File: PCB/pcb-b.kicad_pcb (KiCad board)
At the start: 2 copper layers, 109.8 x 43.6 mm, 93 parts, among them J1 IXTP3N50D2, Q1 BC817, Q10 BC817, Q11 TPCA8120,L1Q, Q12 BC817, Q13 TPCA8120,L1Q, Q14 BC817, Q15 BC817, Q16 BC817, Q17 BC327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

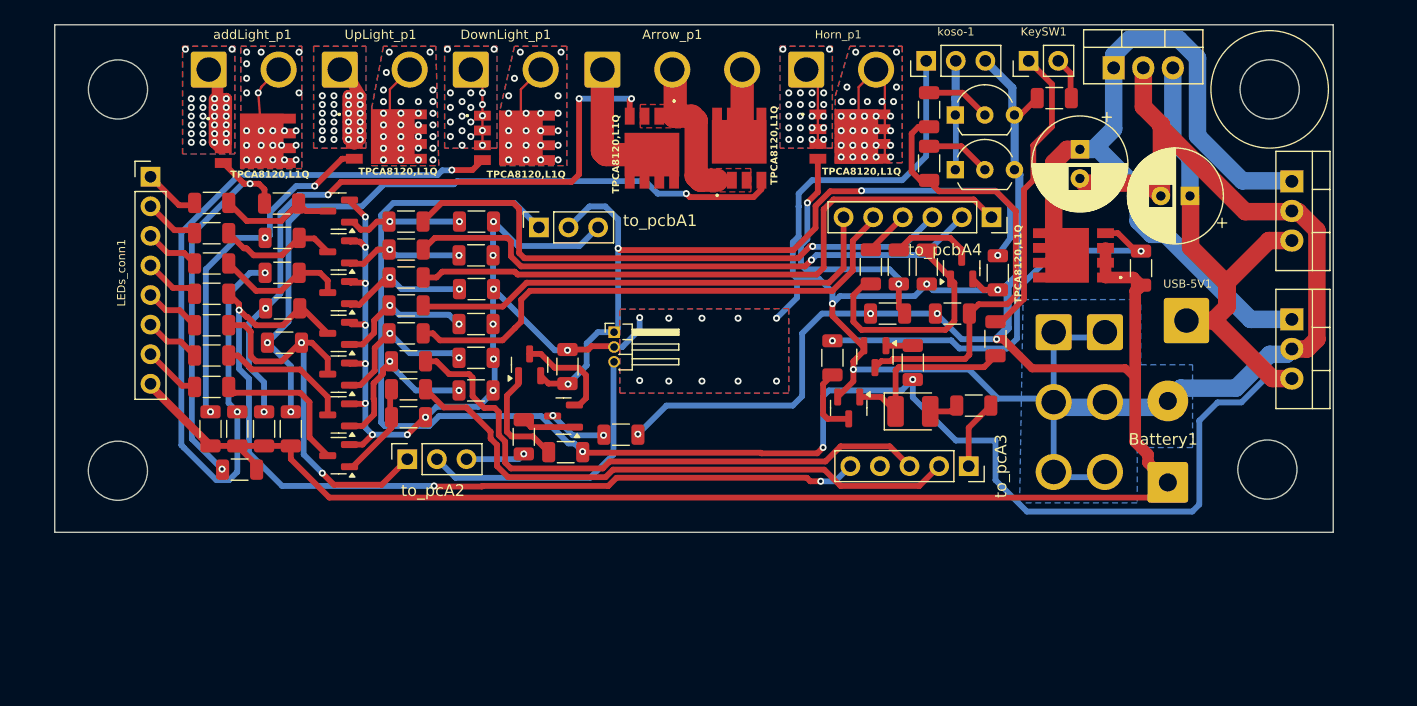
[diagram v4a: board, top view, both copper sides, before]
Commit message: With mechanical relay version
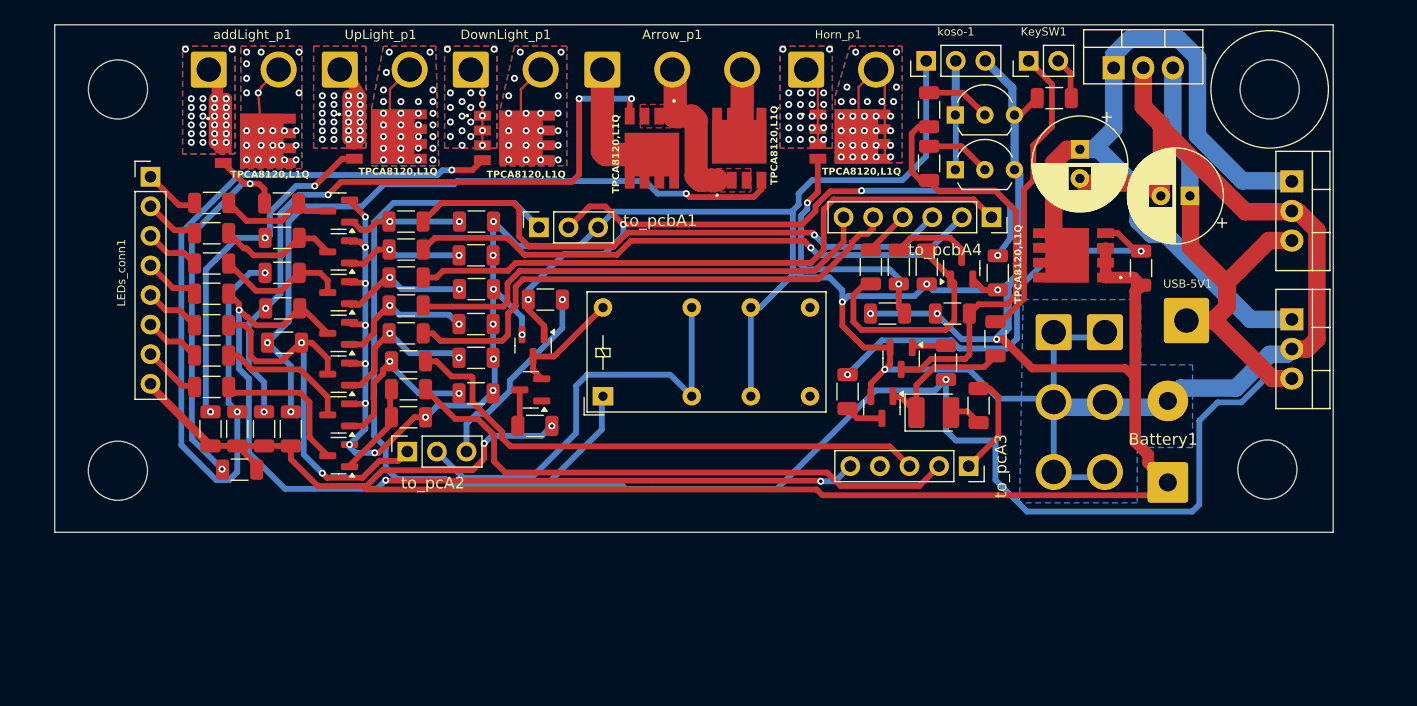
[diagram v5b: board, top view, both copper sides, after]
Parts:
- removed J1: IXTP3N50D2, Connector_PinHeader_1.27mm:PinHeader_1x03_P1.27mm_Horizontal
- removed RA23: 10K, Resistor_SMD:R_1206_3216Metric
- removed RA29: 3K, Resistor_SMD:R_1206_3216Metric
- added K1: HK19F-DCxxV-SHC, Relay_THT:Relay_DPDT_Finder_30.22, F.Cu at (149.2, 102.2)
- moved RA44 11.9 mm to (144.3, 93.8), turned to 180 degrees
- moved RA43 7.43 mm to (143.4, 104.7)
- moved Q16 3.60 mm to (143.1, 101.6)
- moved R3 3.18 mm to (170.2, 101.8)
- moved Q9 2.85 mm to (173.2, 103.1)
- moved RA8 2.85 mm to (178.7, 99.2)
- moved Q10 2.25 mm to (174.8, 98.9)
- moved D1 1.79 mm to (177.7, 103.5)
- moved Q12 1.68 mm to (143.2, 97.8), turned to -90 degrees
- moved to_pcA2 0.65 mm to (132.4, 106.9)
- moved R5 0.41 mm to (181.5, 103.0), turned to 90 degrees
- moved RA39 0.25 mm to (138.3, 101.9)
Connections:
- Q12 pad 1: Net-(Q12-B) -> i_powerOFF
- Q12 pad 2: i_powerOFF -> GND
- RA44 pad 2: Net-(Q16-B) -> i_powerOFF
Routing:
- net GND: track 259.8 -> 274.6 mm, vias 30 -> 20
- net tempPower: track 180.9 -> 194.0 mm, vias 3 -> 1
- net c_engineOFF: track 24.6 -> 37.2 mm
- net o_engineON: track 5.11 -> 17.0 mm
- net Net-(Q12-B): track 9.54 -> 0.00 mm
- net +12V: track 201.8 -> 193.2 mm, vias 4 -> 5
- net i_powerOFF: track 67.0 -> 61.3 mm
- net Net-(Q16-B): track 4.61 -> 0.00 mm
- net Net-(D1-K): track 16.2 -> 12.8 mm
- net o_neutral: track 50.0 -> 46.8 mm
- net o_keepAlive: track 5.99 -> 9.00 mm
- net Net-(Q9-C): track 6.08 -> 3.29 mm
- net Net-(Q10-C): track 39.4 -> 37.2 mm
- net Net-(Q16-C): track 5.05 -> 3.17 mm, vias 2 -> 0
- net Net-(Q12-C): track 8.81 -> 9.96 mm
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- removed copper zone on F.Cu, net GND

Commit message: small changes
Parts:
- moved USB-5V1 1.72 mm to (197.9, 96.7)
- moved Battery1 1.10 mm to (196.7, 109.5)
- moved GND-1 0.73 mm to (191.7, 96.5)
- moved GND-2 0.73 mm to (187.2, 96.5)
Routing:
- net tempPower: track 194.0 -> 197.4 mm
- net GND: track 274.6 -> 272.0 mm
- net +12V: track 193.2 -> 191.5 mm

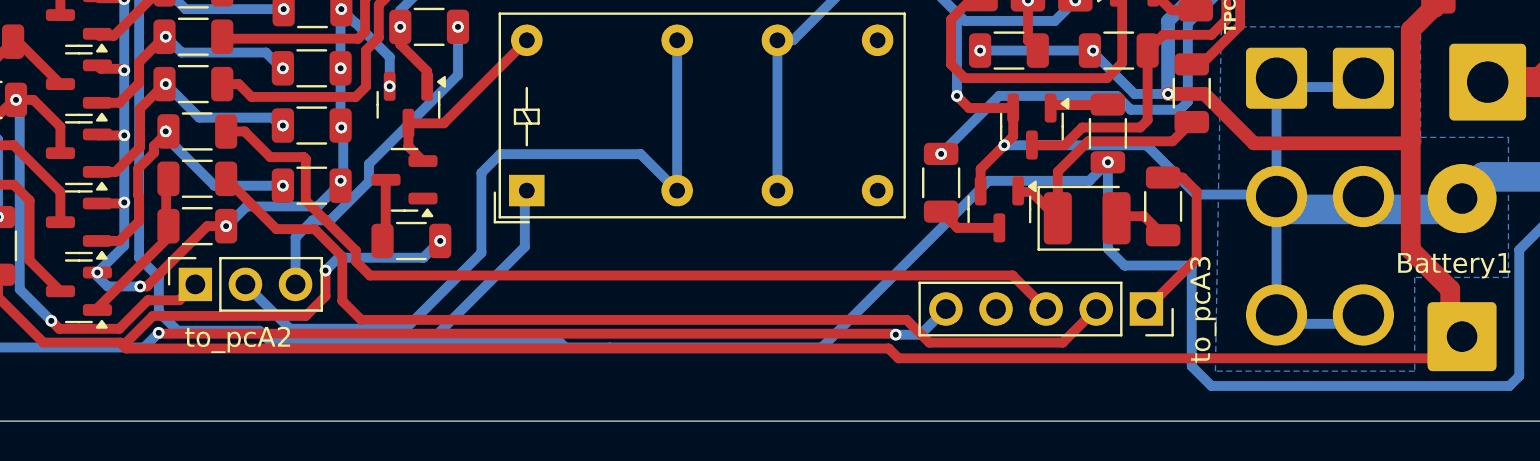
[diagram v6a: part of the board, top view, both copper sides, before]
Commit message: Wrong relay's power supply fixed
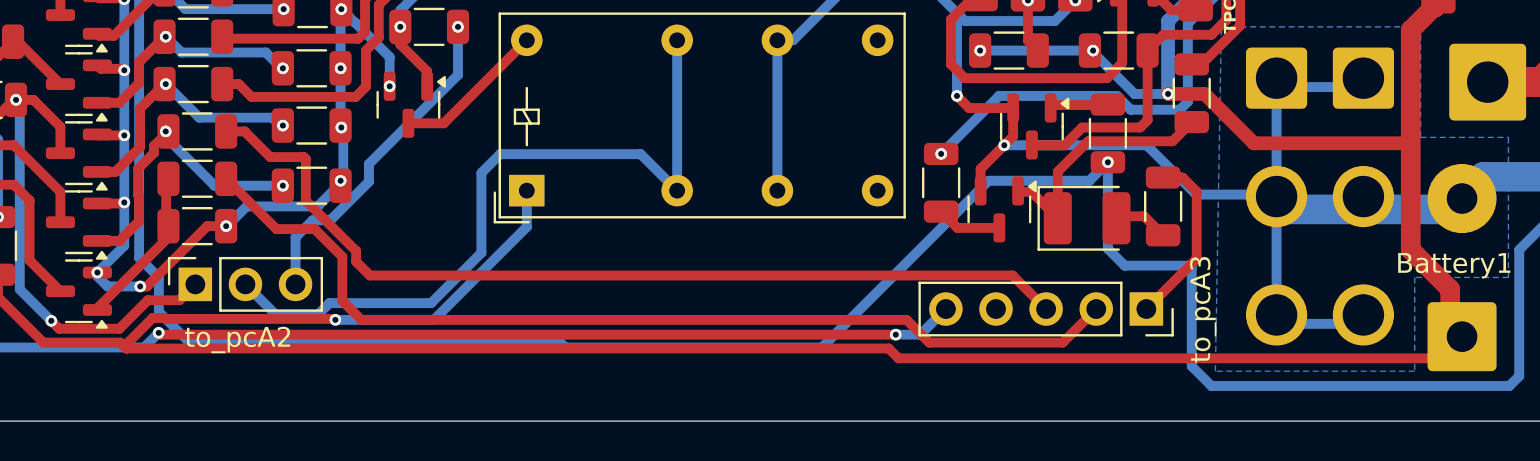
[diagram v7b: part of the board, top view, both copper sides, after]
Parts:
- removed Q16: BC817, Package_TO_SOT_SMD:SOT-23
- removed RA43: 3K, Resistor_SMD:R_1206_3216Metric
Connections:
- K1 pad A1: tempPower -> +12V
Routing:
- net tempPower: track 197.4 -> 187.6 mm
- net +12V: track 191.5 -> 197.2 mm, vias 5 -> 4
- net Net-(Q16-C): track 3.17 -> 0.00 mm
- net Net-(Q12-C): track 9.96 -> 7.74 mm
- net c_engineOFF: track 37.2 -> 36.7 mm

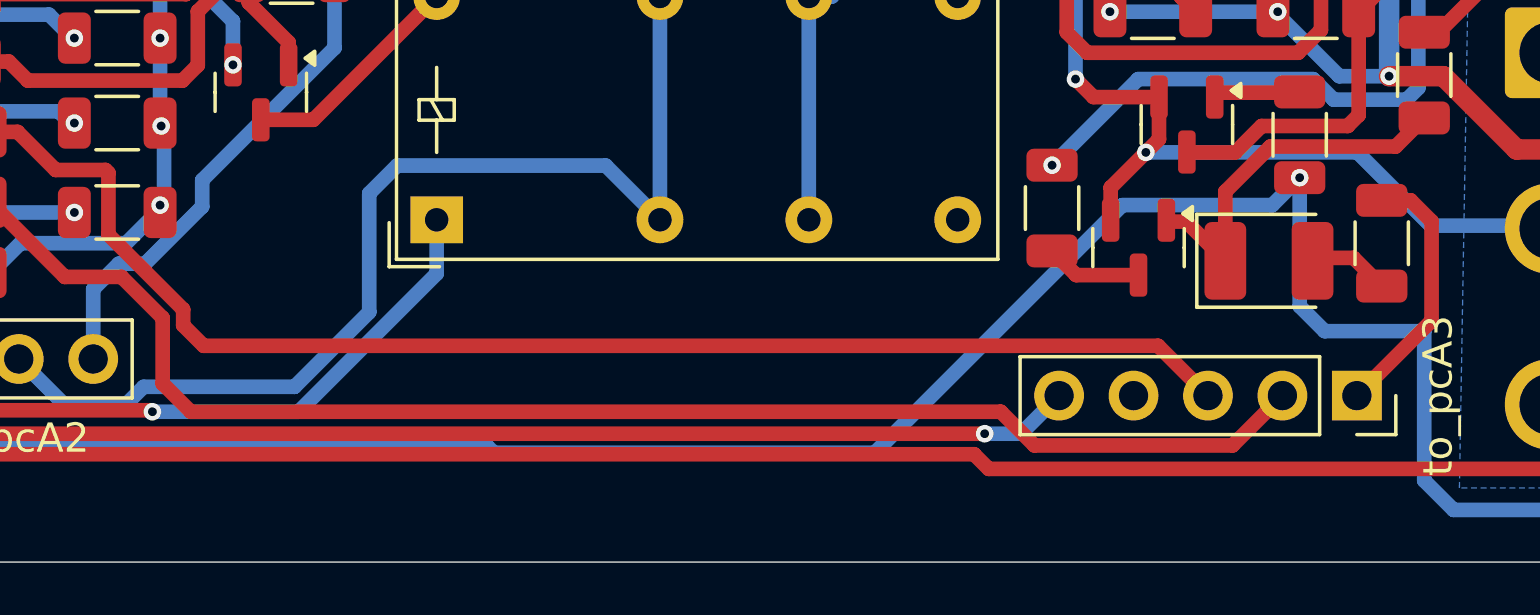
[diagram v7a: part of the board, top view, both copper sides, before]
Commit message: Pull-down resistor missing fixed
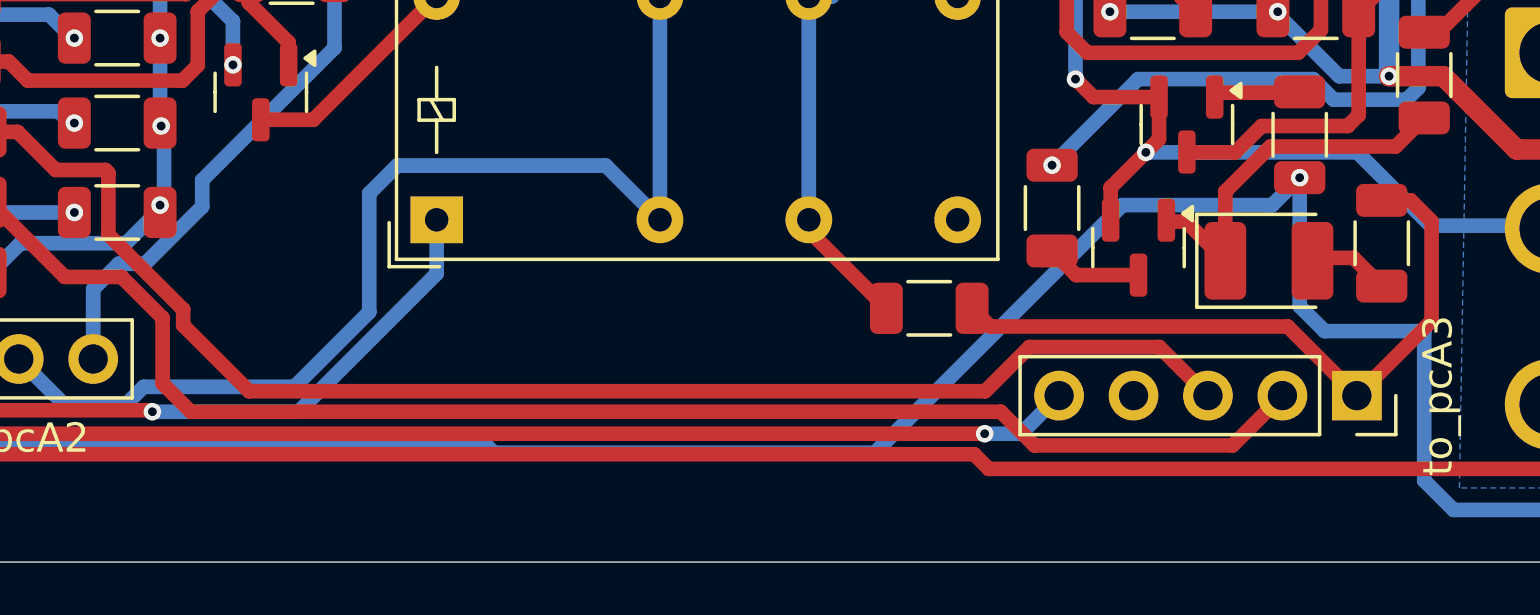
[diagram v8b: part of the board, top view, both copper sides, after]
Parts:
- added R6: 33K, Resistor_SMD:R_1206_3216Metric, F.Cu at (166.1, 105.2)
- R1, R4: value 5K -> 15K
- R5: value 5K -> 33K
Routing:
- net o_keepAlive: track 9.00 -> 23.4 mm
- net GND: track 272.0 -> 276.1 mm
- net o_neutral: track 46.8 -> 48.1 mm
